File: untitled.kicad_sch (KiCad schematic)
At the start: 1 part

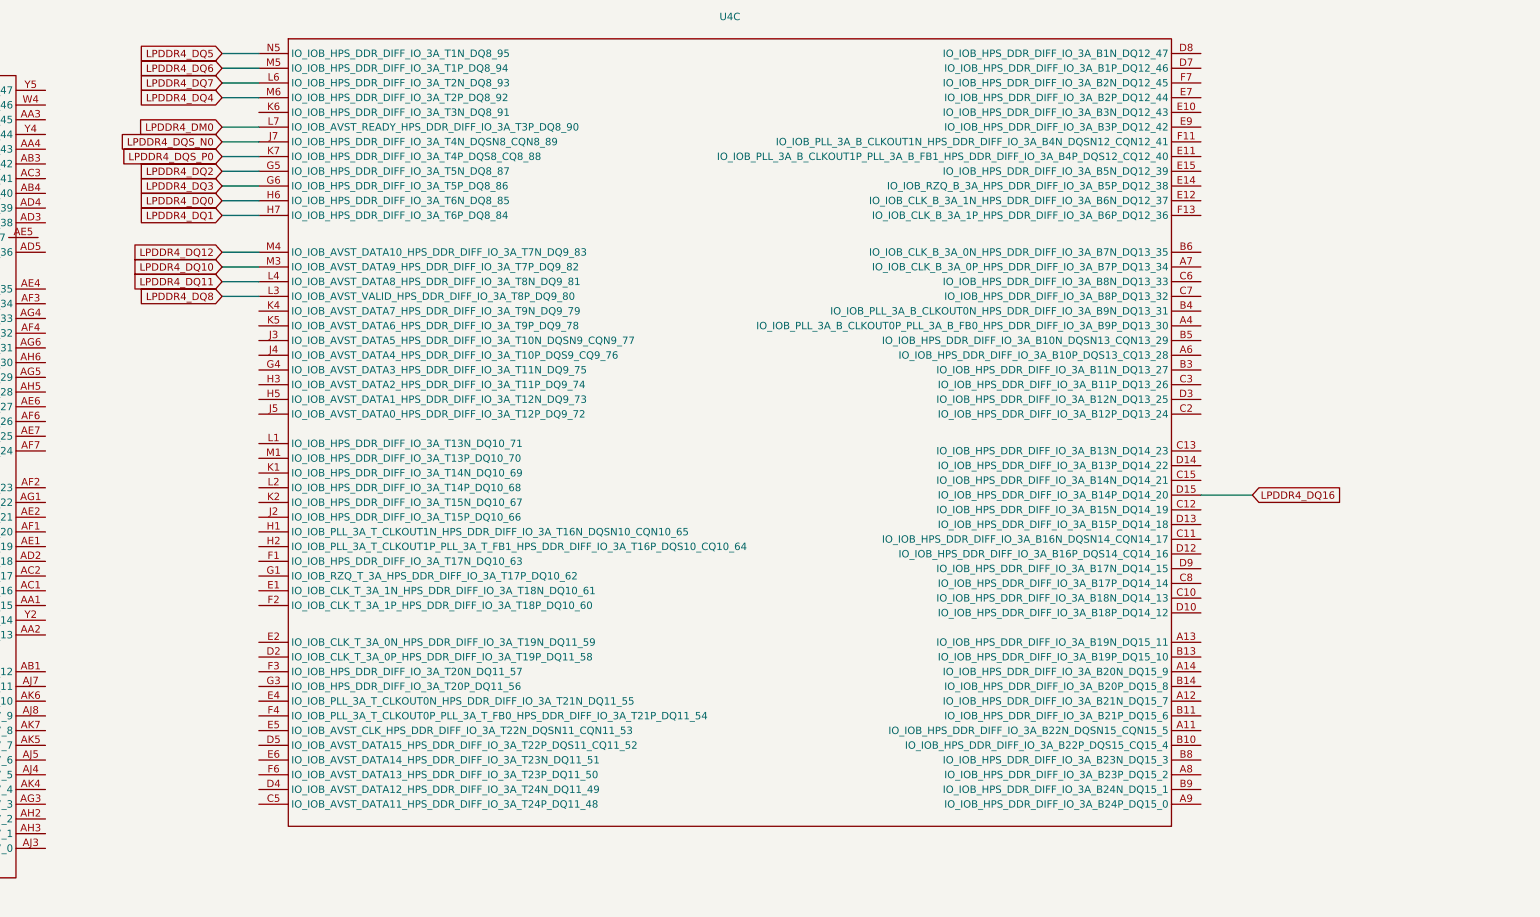
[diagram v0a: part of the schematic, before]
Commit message: add lpddr4 connections in schematic
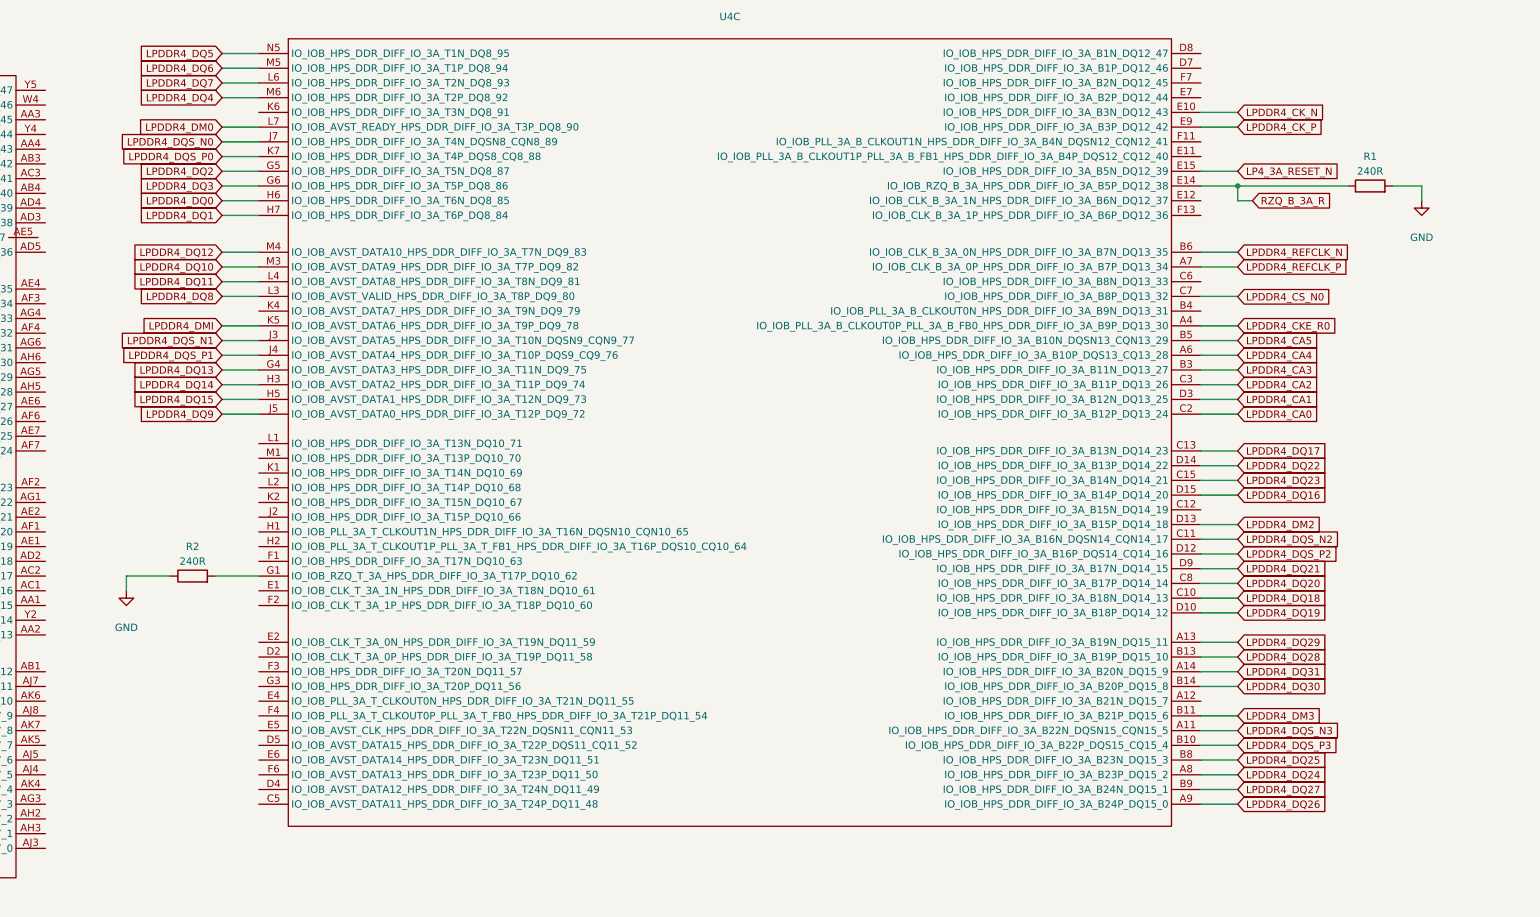
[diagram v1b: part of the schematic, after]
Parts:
- added R1: 240R, Resistor_SMD:R_0402_1005Metric, symbol Device:R
- added R2: 240R, symbol Device:R
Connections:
- net LPDDR4_DQS_N3: now reaches U4.A11 (IO_IOB_HPS_DDR_DIFF_IO_3A_B22N_DQSN15_CQN15_5)
- net LPDDR4_DQ29: now reaches U4.A13 (IO_IOB_HPS_DDR_DIFF_IO_3A_B19N_DQ15_11)
- net LPDDR4_DQ31: now reaches U4.A14 (IO_IOB_HPS_DDR_DIFF_IO_3A_B20N_DQ15_9)
- net LPDDR4_CKE_R0: now reaches U4.A4 (IO_IOB_PLL_3A_B_CLKOUT0P_PLL_3A_B_FB0_HPS_DDR_DIFF_IO_3A_B9P_DQ13_30)
- net LPDDR4_CA4: now reaches U4.A6 (IO_IOB_HPS_DDR_DIFF_IO_3A_B10P_DQS13_CQ13_28)
- net LPDDR4_REFCLK_P: now reaches U4.A7 (IO_IOB_CLK_B_3A_0P_HPS_DDR_DIFF_IO_3A_B7P_DQ13_34)
- net LPDDR4_DQ24: now reaches U4.A8 (IO_IOB_HPS_DDR_DIFF_IO_3A_B23P_DQ15_2)
- net LPDDR4_DQ26: now reaches U4.A9 (IO_IOB_HPS_DDR_DIFF_IO_3A_B24P_DQ15_0)
- net LPDDR4_DQS_P3: now reaches U4.B10 (IO_IOB_HPS_DDR_DIFF_IO_3A_B22P_DQS15_CQ15_4)
- net LPDDR4_DM3: now reaches U4.B11 (IO_IOB_HPS_DDR_DIFF_IO_3A_B21P_DQ15_6)
- net LPDDR4_DQ28: now reaches U4.B13 (IO_IOB_HPS_DDR_DIFF_IO_3A_B19P_DQ15_10)
- net LPDDR4_DQ30: now reaches U4.B14 (IO_IOB_HPS_DDR_DIFF_IO_3A_B20P_DQ15_8)
- net LPDDR4_CA3: now reaches U4.B3 (IO_IOB_HPS_DDR_DIFF_IO_3A_B11N_DQ13_27)
- net LPDDR4_CA5: now reaches U4.B5 (IO_IOB_HPS_DDR_DIFF_IO_3A_B10N_DQSN13_CQN13_29)
- net LPDDR4_REFCLK_N: now reaches U4.B6 (IO_IOB_CLK_B_3A_0N_HPS_DDR_DIFF_IO_3A_B7N_DQ13_35)
- net LPDDR4_DQ25: now reaches U4.B8 (IO_IOB_HPS_DDR_DIFF_IO_3A_B23N_DQ15_3)
- net LPDDR4_DQ27: now reaches U4.B9 (IO_IOB_HPS_DDR_DIFF_IO_3A_B24N_DQ15_1)
- net LPDDR4_DQ18: now reaches U4.C10 (IO_IOB_HPS_DDR_DIFF_IO_3A_B18N_DQ14_13)
- net LPDDR4_DQS_N2: now reaches U4.C11 (IO_IOB_HPS_DDR_DIFF_IO_3A_B16N_DQSN14_CQN14_17)
- net LPDDR4_DQ17: now reaches U4.C13 (IO_IOB_HPS_DDR_DIFF_IO_3A_B13N_DQ14_23)
- net LPDDR4_DQ23: now reaches U4.C15 (IO_IOB_HPS_DDR_DIFF_IO_3A_B14N_DQ14_21)
- net LPDDR4_CA0: now reaches U4.C2 (IO_IOB_HPS_DDR_DIFF_IO_3A_B12P_DQ13_24)
- net LPDDR4_CA2: now reaches U4.C3 (IO_IOB_HPS_DDR_DIFF_IO_3A_B11P_DQ13_26)
- net LPDDR4_DQ20: now reaches U4.C8 (IO_IOB_HPS_DDR_DIFF_IO_3A_B17P_DQ14_14)
- net LPDDR4_DQ19: now reaches U4.D10 (IO_IOB_HPS_DDR_DIFF_IO_3A_B18P_DQ14_12)
- net LPDDR4_DQS_P2: now reaches U4.D12 (IO_IOB_HPS_DDR_DIFF_IO_3A_B16P_DQS14_CQ14_16)
- net LPDDR4_DM2: now reaches U4.D13 (IO_IOB_HPS_DDR_DIFF_IO_3A_B15P_DQ14_18)
- net LPDDR4_DQ22: now reaches U4.D14 (IO_IOB_HPS_DDR_DIFF_IO_3A_B13P_DQ14_22)
- net LPDDR4_CA1: now reaches U4.D3 (IO_IOB_HPS_DDR_DIFF_IO_3A_B12N_DQ13_25)
- net LPDDR4_DQ21: now reaches U4.D9 (IO_IOB_HPS_DDR_DIFF_IO_3A_B17N_DQ14_15)
- net LPDDR4_CK_N: now reaches U4.E10 (IO_IOB_HPS_DDR_DIFF_IO_3A_B3N_DQ12_43)
- net RZQ_B_3A_R: now reaches U4.E14 (IO_IOB_RZQ_B_3A_HPS_DDR_DIFF_IO_3A_B5P_DQ12_38)
- net RZQ_B_3A_R: now also R1.1
- net LP4_3A_RESET_N: now reaches U4.E15 (IO_IOB_HPS_DDR_DIFF_IO_3A_B5N_DQ12_39)
- net LPDDR4_CK_P: now reaches U4.E9 (IO_IOB_HPS_DDR_DIFF_IO_3A_B3P_DQ12_42)
- net at U4.G1 (IO_IOB_RZQ_T_3A_HPS_DDR_DIFF_IO_3A_T17P_DQ10_62): now also R2.2
- net LPDDR4_DQ13: now reaches U4.G4 (IO_IOB_AVST_DATA3_HPS_DDR_DIFF_IO_3A_T11N_DQ9_75)
- net LPDDR4_DQ14: now reaches U4.H3 (IO_IOB_AVST_DATA2_HPS_DDR_DIFF_IO_3A_T11P_DQ9_74)
- net LPDDR4_DQ15: now reaches U4.H5 (IO_IOB_AVST_DATA1_HPS_DDR_DIFF_IO_3A_T12N_DQ9_73)
- net LPDDR4_DQS_N1: now reaches U4.J3 (IO_IOB_AVST_DATA5_HPS_DDR_DIFF_IO_3A_T10N_DQSN9_CQN9_77)
- net LPDDR4_DQS_P1: now reaches U4.J4 (IO_IOB_AVST_DATA4_HPS_DDR_DIFF_IO_3A_T10P_DQS9_CQ9_76)
- net LPDDR4_DQ9: now reaches U4.J5 (IO_IOB_AVST_DATA0_HPS_DDR_DIFF_IO_3A_T12P_DQ9_72)
- net LPDDR4_DMI: now reaches U4.K5 (IO_IOB_AVST_DATA6_HPS_DDR_DIFF_IO_3A_T9P_DQ9_78)
- new net GND: R1.2, R2.1

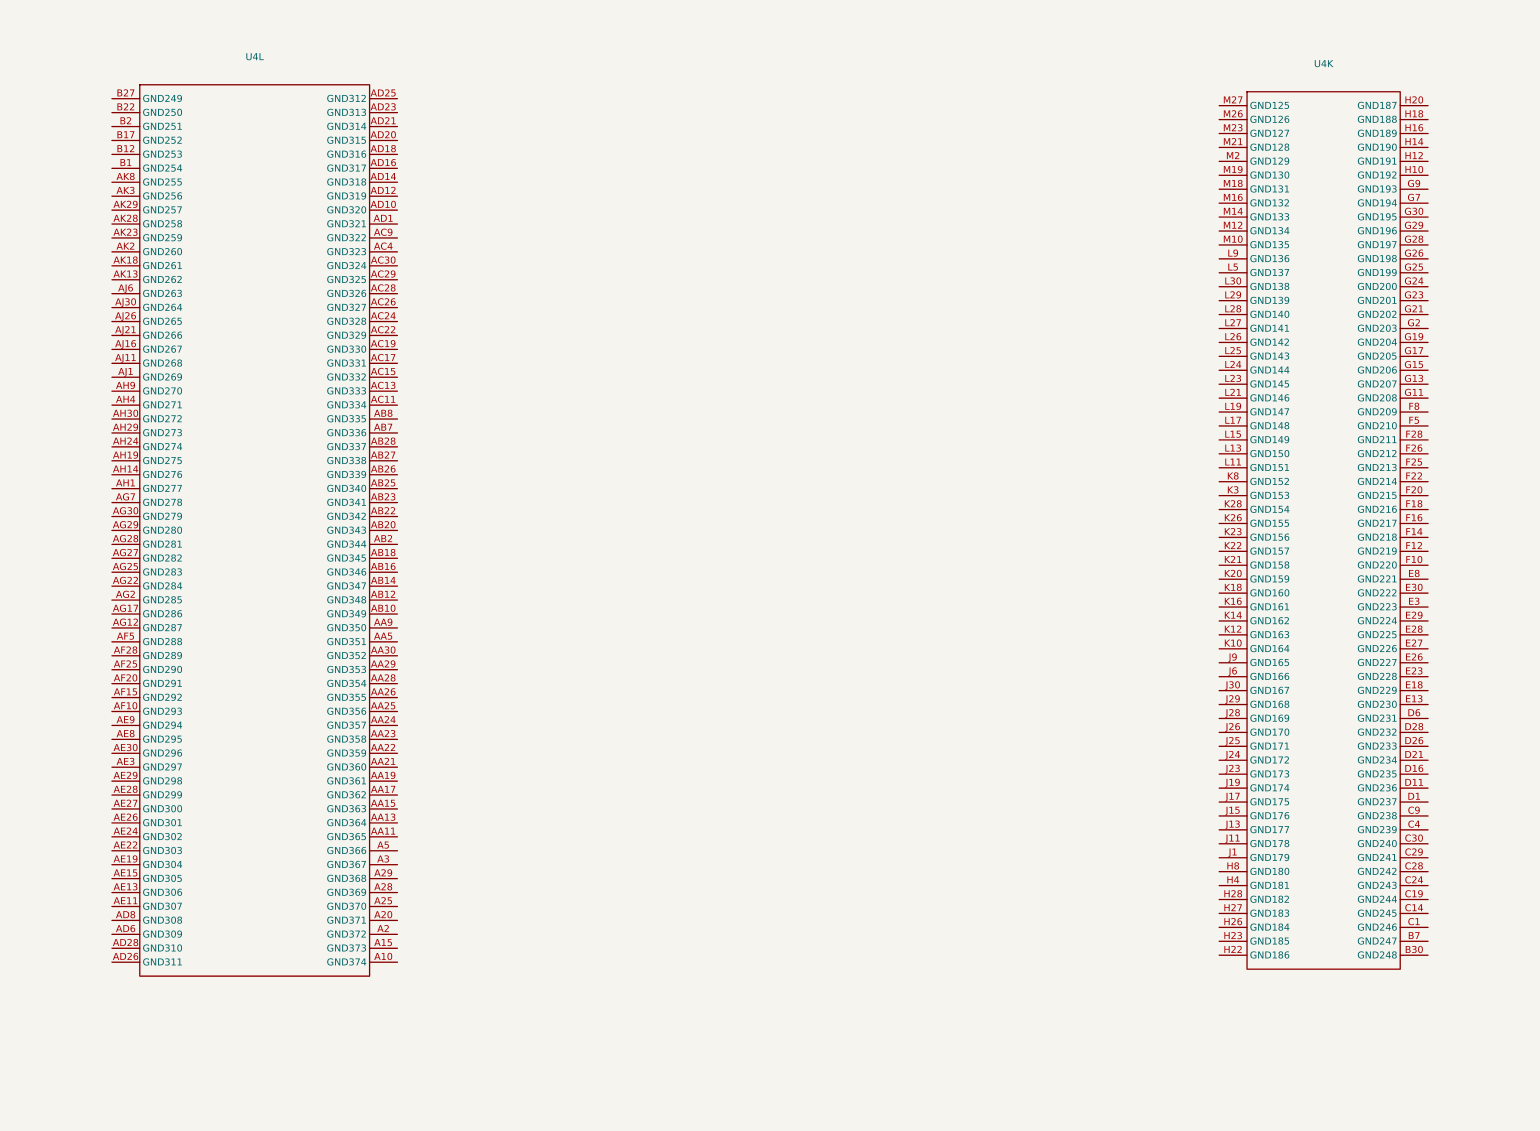
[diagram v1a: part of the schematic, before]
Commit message: start making agilex 5 b23b package
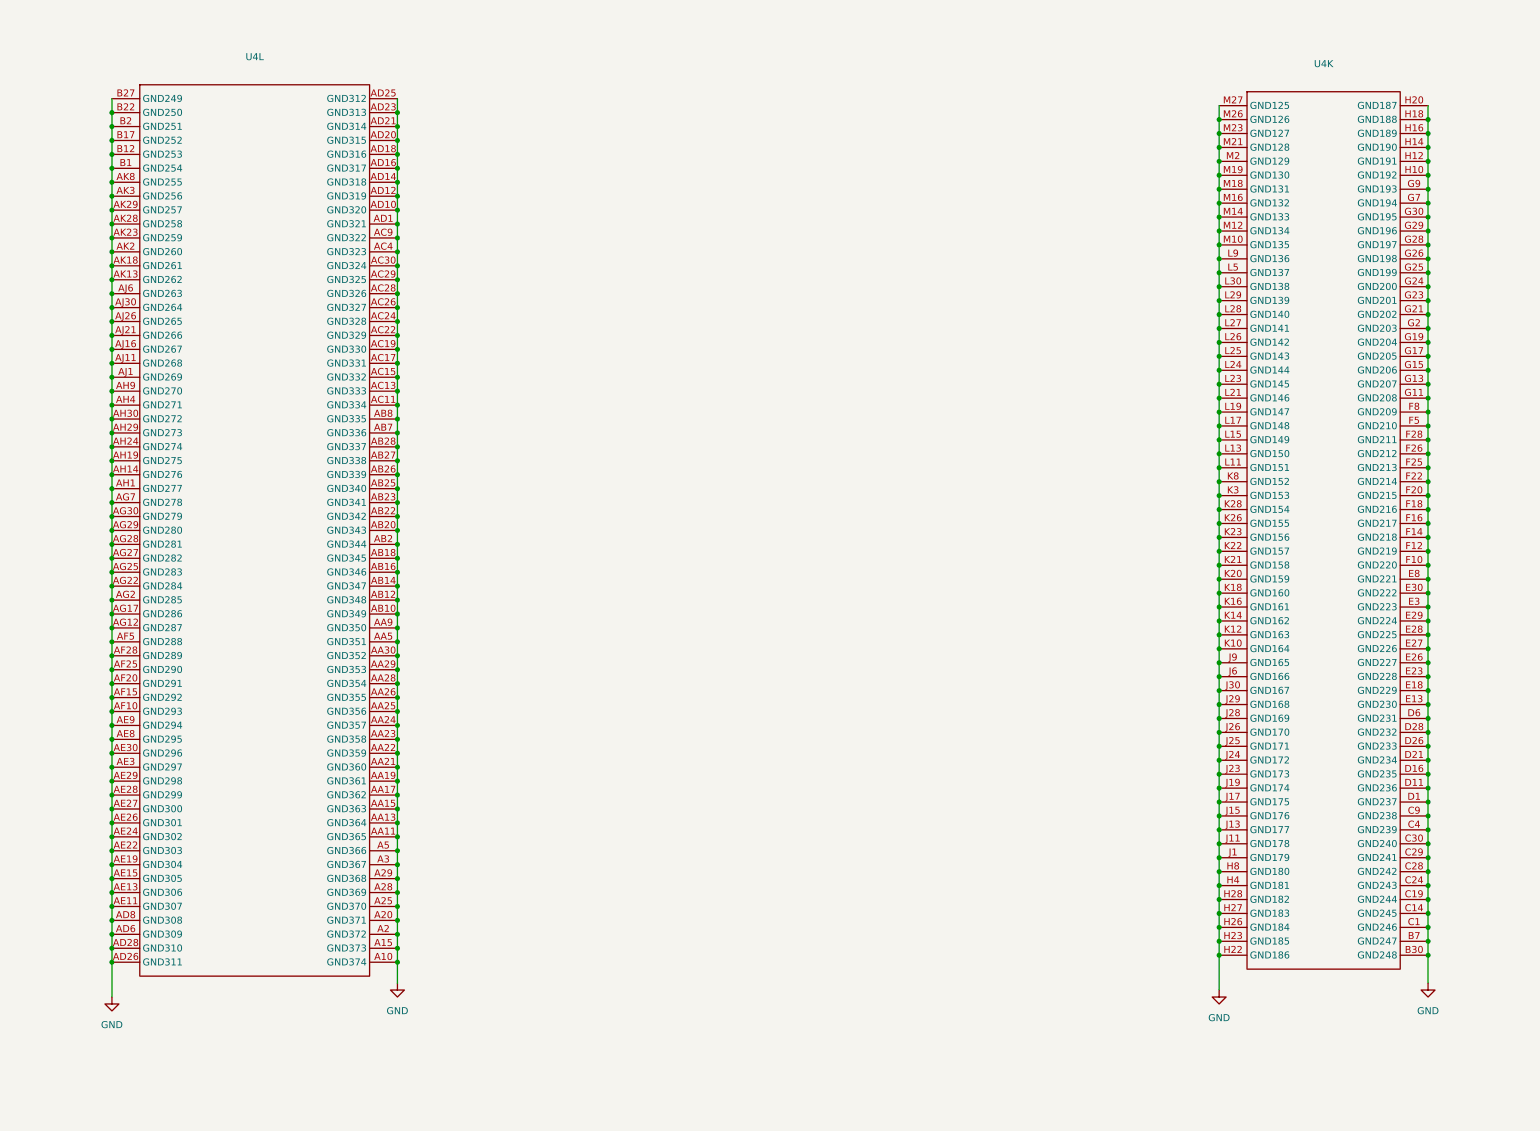
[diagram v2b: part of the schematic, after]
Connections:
- net GND: now also U4.A10 (GND374), U4.A15 (GND373), U4.A2 (GND372), U4.A20 (GND371), U4.A25 (GND370), U4.A28 (GND369), U4.A29 (GND368), U4.A3 (GND367), U4.A5 (GND366), U4.AA11 (GND365), U4.AA13 (GND364), U4.AA15 (GND363), U4.AA17 (GND362), U4.AA19 (GND361), U4.AA21 (GND360), U4.AA22 (GND359), U4.AA23 (GND358), U4.AA24 (GND357), U4.AA25 (GND356), U4.AA26 (GND355), U4.AA28 (GND354), U4.AA29 (GND353), U4.AA30 (GND352), U4.AA5 (GND351), U4.AA9 (GND350), U4.AB10 (GND349), U4.AB12 (GND348), U4.AB14 (GND347), U4.AB16 (GND346), U4.AB18 (GND345), U4.AB2 (GND344), U4.AB20 (GND343), U4.AB22 (GND342), U4.AB23 (GND341), U4.AB25 (GND340), U4.AB26 (GND339), U4.AB27 (GND338), U4.AB28 (GND337), U4.AB7 (GND336), U4.AB8 (GND335), U4.AC11 (GND334), U4.AC13 (GND333), U4.AC15 (GND332), U4.AC17 (GND331), U4.AC19 (GND330), U4.AC22 (GND329), U4.AC24 (GND328), U4.AC26 (GND327), U4.AC28 (GND326), U4.AC29 (GND325), U4.AC30 (GND324), U4.AC4 (GND323), U4.AC9 (GND322), U4.AD1 (GND321), U4.AD10 (GND320), U4.AD12 (GND319), U4.AD14 (GND318), U4.AD16 (GND317), U4.AD18 (GND316), U4.AD20 (GND315), U4.AD21 (GND314), U4.AD23 (GND313), U4.AD25 (GND312), U4.AD26 (GND311), U4.AD28 (GND310), U4.AD6 (GND309), U4.AD8 (GND308), U4.AE11 (GND307), U4.AE13 (GND306), U4.AE15 (GND305), U4.AE19 (GND304), U4.AE22 (GND303), U4.AE24 (GND302), U4.AE26 (GND301), U4.AE27 (GND300), U4.AE28 (GND299), U4.AE29 (GND298), U4.AE3 (GND297), U4.AE30 (GND296), U4.AE8 (GND295), U4.AE9 (GND294), U4.AF10 (GND293), U4.AF15 (GND292), U4.AF20 (GND291), U4.AF25 (GND290), U4.AF28 (GND289), U4.AF5 (GND288), U4.AG12 (GND287), U4.AG17 (GND286), U4.AG2 (GND285), U4.AG22 (GND284), U4.AG25 (GND283), U4.AG27 (GND282), U4.AG28 (GND281), U4.AG29 (GND280), U4.AG30 (GND279), U4.AG7 (GND278), U4.AH1 (GND277), U4.AH14 (GND276), U4.AH19 (GND275), U4.AH24 (GND274), U4.AH29 (GND273), U4.AH30 (GND272), U4.AH4 (GND271), U4.AH9 (GND270), U4.AJ1 (GND269), U4.AJ11 (GND268), U4.AJ16 (GND267), U4.AJ21 (GND266), U4.AJ26 (GND265), U4.AJ30 (GND264), U4.AJ6 (GND263), U4.AK13 (GND262), U4.AK18 (GND261), U4.AK2 (GND260), U4.AK23 (GND259), U4.AK28 (GND258), U4.AK29 (GND257), U4.AK3 (GND256), U4.AK8 (GND255), U4.B1 (GND254), U4.B12 (GND253), U4.B17 (GND252), U4.B2 (GND251), U4.B22 (GND250), U4.B27 (GND249), U4.B30 (GND248), U4.B7 (GND247), U4.C1 (GND246), U4.C14 (GND245), U4.C19 (GND244), U4.C24 (GND243), U4.C28 (GND242), U4.C29 (GND241), U4.C30 (GND240), U4.C4 (GND239), U4.C9 (GND238), U4.D1 (GND237), U4.D11 (GND236), U4.D16 (GND235), U4.D21 (GND234), U4.D26 (GND233), U4.D28 (GND232), U4.D6 (GND231), U4.E13 (GND230), U4.E18 (GND229), U4.E23 (GND228), U4.E26 (GND227), U4.E27 (GND226), U4.E28 (GND225), U4.E29 (GND224), U4.E3 (GND223), U4.E30 (GND222), U4.E8 (GND221), U4.F10 (GND220), U4.F12 (GND219), U4.F14 (GND218), U4.F16 (GND217), U4.F18 (GND216), U4.F20 (GND215), U4.F22 (GND214), U4.F25 (GND213), U4.F26 (GND212), U4.F28 (GND211), U4.F5 (GND210), U4.F8 (GND209), U4.G11 (GND208), U4.G13 (GND207), U4.G15 (GND206), U4.G17 (GND205), U4.G19 (GND204), U4.G2 (GND203), U4.G21 (GND202), U4.G23 (GND201), U4.G24 (GND200), U4.G25 (GND199), U4.G26 (GND198), U4.G28 (GND197), U4.G29 (GND196), U4.G30 (GND195), U4.G7 (GND194), U4.G9 (GND193), U4.H10 (GND192), U4.H12 (GND191), U4.H14 (GND190), U4.H16 (GND189), U4.H18 (GND188), U4.H20 (GND187), U4.H22 (GND186), U4.H23 (GND185), U4.H26 (GND184), U4.H27 (GND183), U4.H28 (GND182), U4.H4 (GND181), U4.H8 (GND180), U4.J1 (GND179), U4.J11 (GND178), U4.J13 (GND177), U4.J15 (GND176), U4.J17 (GND175), U4.J19 (GND174), U4.J23 (GND173), U4.J24 (GND172), U4.J25 (GND171), U4.J26 (GND170), U4.J28 (GND169), U4.J29 (GND168), U4.J30 (GND167), U4.J6 (GND166), U4.J9 (GND165), U4.K10 (GND164), U4.K12 (GND163), U4.K14 (GND162), U4.K16 (GND161), U4.K18 (GND160), U4.K20 (GND159), U4.K21 (GND158), U4.K22 (GND157), U4.K23 (GND156), U4.K26 (GND155), U4.K28 (GND154), U4.K3 (GND153), U4.K8 (GND152), U4.L11 (GND151), U4.L13 (GND150), U4.L15 (GND149), U4.L17 (GND148), U4.L19 (GND147), U4.L21 (GND146), U4.L23 (GND145), U4.L24 (GND144), U4.L25 (GND143), U4.L26 (GND142), U4.L27 (GND141), U4.L28 (GND140), U4.L29 (GND139), U4.L30 (GND138), U4.L5 (GND137), U4.L9 (GND136), U4.M10 (GND135), U4.M12 (GND134), U4.M14 (GND133), U4.M16 (GND132), U4.M18 (GND131), U4.M19 (GND130), U4.M2 (GND129), U4.M21 (GND128), U4.M23 (GND127), U4.M26 (GND126), U4.M27 (GND125)

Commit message: start creating schematic symbol for agilex 5
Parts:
- R2: footprint (none) -> Capacitor_SMD:C_0402_1005Metric
- U4: footprint agilex_lib:BGA-900_30x30_16.0x16.0mm -> agilex_lib:M16A
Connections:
- net t4: now reaches U4.AG3 (IO_IOB_DIFF_IO_2A_B23N_DQ7_3)
- net t5: now reaches U4.AH2 (IO_IOB_DIFF_IO_2A_B23P_DQ7_2)
- net t6: now reaches U4.AH3 (IO_IOB_DIFF_IO_2A_B24N_DQ7_1)
- net t7: now reaches U4.AJ3 (IO_IOB_DIFF_IO_2A_B24P_DQ7_0)
- net t2: now reaches U4.AJ4 (IO_IOB_DIFF_IO_2A_B22N_DQSN7_CQN7_5)
- net t1: now reaches U4.AJ5 (IO_IOB_DIFF_IO_2A_B21P_DQ7_6)
- net t3: now reaches U4.AK4 (IO_IOB_DIFF_IO_2A_B22P_DQS7_CQ7_4)

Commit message: add agilex 5 schematic files
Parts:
- U4: value ~ -> (none)
